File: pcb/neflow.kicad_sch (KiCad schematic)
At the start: 51 parts, among them J1 Temp0, J2 Temp1, J3 SSR0, J4 SSR1, J6 1333870, J7 FAN1, J8 FAN0, Q1 IRLML2502, Q2 IRLML2502, Q3 IRLML2502, Q4 IRLML2502, Q5 IRLML2502, Q6 Q_PMOS_GSD, SW1 SW_Push, SW2 SW_Push, SW3 SW_Push, SW4 SW_Push, U1 MAX31855KASA+T, U2 MAX31855KASA+T, U3 Pico

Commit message: WIP: Switching to workstation
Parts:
- added R1, R11: 10K, Resistor_SMD:R_0603_1608Metric, symbol Device:R_Small
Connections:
- net +3.3V: now also U3.36 (3V3), R1.2, R11.2
- net MAX_SO: now reaches U3.11 (GPIO8)
- net MAX_SO: now also U1.7 (SO), U2.7 (SO)
- net PI_TEMP0_~{CS}: now reaches U3.14 (GPIO10)
- net PI_TEMP0_~{CS}: now also U1.6 (~{CS}), R1.1
- net PI_TEMP1_~{CS}: now reaches U3.15 (GPIO11)
- net PI_TEMP1_~{CS}: now also U2.6 (~{CS}), R11.1
- net SCREEN_SDA: now reaches U3.4 (GPIO2)
- net SCREEN_SDA: now also Brd1.4 (SDA)
- net SCREEN_SCL: now reaches U3.5 (GPIO3)
- net SCREEN_SCL: now also Brd1.3 (SCL)
- net MAX_SCK: now reaches U3.9 (GPIO6)
- net MAX_SCK: now also U1.5 (SCK), U2.5 (SCK)
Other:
- moved on the sheet: C1, C2, C3, C4, C5, C6, FB1, FB2, FB3, FB4, J1, J2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

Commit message: WIP: Working on pcb
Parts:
- J101: renamed from J6; footprint Unsharable:1333870 -> Unshareable:1333870
- JP102: renamed from JP2; value SolderJumper_3_Open -> VSel1
- renumbered Brd1 to Brd101, C7 to C101, C8 to C102, C9 to C103, C10 to C104, C2 to C105, C3 to C106, C5 to C107, C6 to C108, C1 to C109, C4 to C110, D1 to D101, D2 to D102, D3 to D103, FB2 to FB101, FB3 to FB102, FB1 to FB103, FB4 to FB104, J8 to J102, J3 to J103, J7 to J104, J4 to J105, J1 to J106, J2 to J107, JP1 to JP101, LS1 to LS101, PS1 to PS101, Q6 to Q101, Q1 to Q102, Q4 to Q103, Q5 to Q104, Q2 to Q105, Q3 to Q106, R7 to R101, R9 to R102, R2 to R103, R5 to R104, R6 to R105, R8 to R106, R10 to R107, R3 to R108, R4 to R109, R1 to R110, R11 to R111, SW1 to SW101, SW3 to SW102, SW2 to SW103, SW4 to SW104, U3 to U101, U1 to U102, U2 to U103
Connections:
- net BTN0: now also U101.16 (GPIO12)
- net BTN1: now also U101.17 (GPIO13)
- net BTN2: now also U101.19 (GPIO14)
- net BTN3: now also U101.20 (GPIO15)
- net FAN0: now also U101.26 (GPIO20)
- net FAN1: now also U101.27 (GPIO21)
- net SPK: now also U101.21 (GPIO16)
- net SSR0: now also U101.24 (GPIO18)
- net SSR1: now also U101.25 (GPIO19)
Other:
- moved on the sheet: C107, C108, C110, FB102, FB104, J107, R107, R111, SW104, U103

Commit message: WIP: changes to pcb
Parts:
- added H1, H2, H3, H4: MountingHole, MountingHole:MountingHole_3mm, symbol Mechanical:MountingHole
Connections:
- net T0+: now also J106.1 (Pin_1); no longer J106.2 (Pin_2)
- net T0-: now also J106.2 (Pin_2); no longer J106.1 (Pin_1)
- net T1+: now also J107.1 (Pin_1); no longer J107.2 (Pin_2)
- net T1-: now also J107.2 (Pin_2); no longer J107.1 (Pin_1)
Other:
- moved on the sheet: J106, J107, JP102

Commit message: WIP: Finishing the pcb rev0
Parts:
- removed R107: 10K, Resistor_SMD:R_0603_1608Metric, symbol Device:R_Small
- removed SW104: SW_Push, silicone_btn:BUTTON_SILICON, symbol Switch:SW_Push
- added H5, H6, H7, H8: MountingHole, MountingHole:MountingHole_3mm, symbol Mechanical:MountingHole
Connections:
- net BTN3 is gone; now on net SCREEN_SCL: U101.20 (GPIO15)
- net BTN0: now also U101.14 (GPIO10); no longer U101.16 (GPIO12)
- net BTN1: now also U101.15 (GPIO11); no longer U101.17 (GPIO13)
- net BTN2: now also U101.16 (GPIO12); no longer U101.19 (GPIO14)
- net FAN0: now also U101.6 (GPIO4); no longer U101.26 (GPIO20)
- net FAN1: now also U101.7 (GPIO5); no longer U101.27 (GPIO21)
- net GND: now also U101.13 (GND), U101.18 (GND), U101.23 (GND), U101.28 (GND), U101.3 (GND), U101.33 (AGND), U101.38 (GND), U101.42 (GND), U101.8 (GND)
- net PI_TEMP0_~{CS}: now also U101.25 (GPIO19); no longer U101.14 (GPIO10)
- net PI_TEMP1_~{CS}: now also U101.26 (GPIO20); no longer U101.15 (GPIO11)
- net SCREEN_SCL: no longer U101.5 (GPIO3)
- net SCREEN_SDA: now also U101.19 (GPIO14); no longer U101.4 (GPIO2)
- net SPK: now also U101.9 (GPIO6); no longer U101.21 (GPIO16)
- net SSR0: now also U101.4 (GPIO2); no longer U101.24 (GPIO18)
- net SSR1: now also U101.5 (GPIO3); no longer U101.25 (GPIO19)
- net AC/L: now reaches J101.1, J101.3, J101.5, PS101.1 (AC/L)
- net AC/N: now reaches J101.2, J101.4, J101.6, PS101.2 (AC/N)
- net MAX_SCK renamed MAX_SPI_SCK
- net MAX_SPI_SCK: now also U101.24 (GPIO18); no longer U101.9 (GPIO6)
- net MAX_SO renamed MAX_SPI_RX
- net MAX_SPI_RX: now also U101.21 (GPIO16); no longer U101.11 (GPIO8)
- no-connect marks 0 -> 15

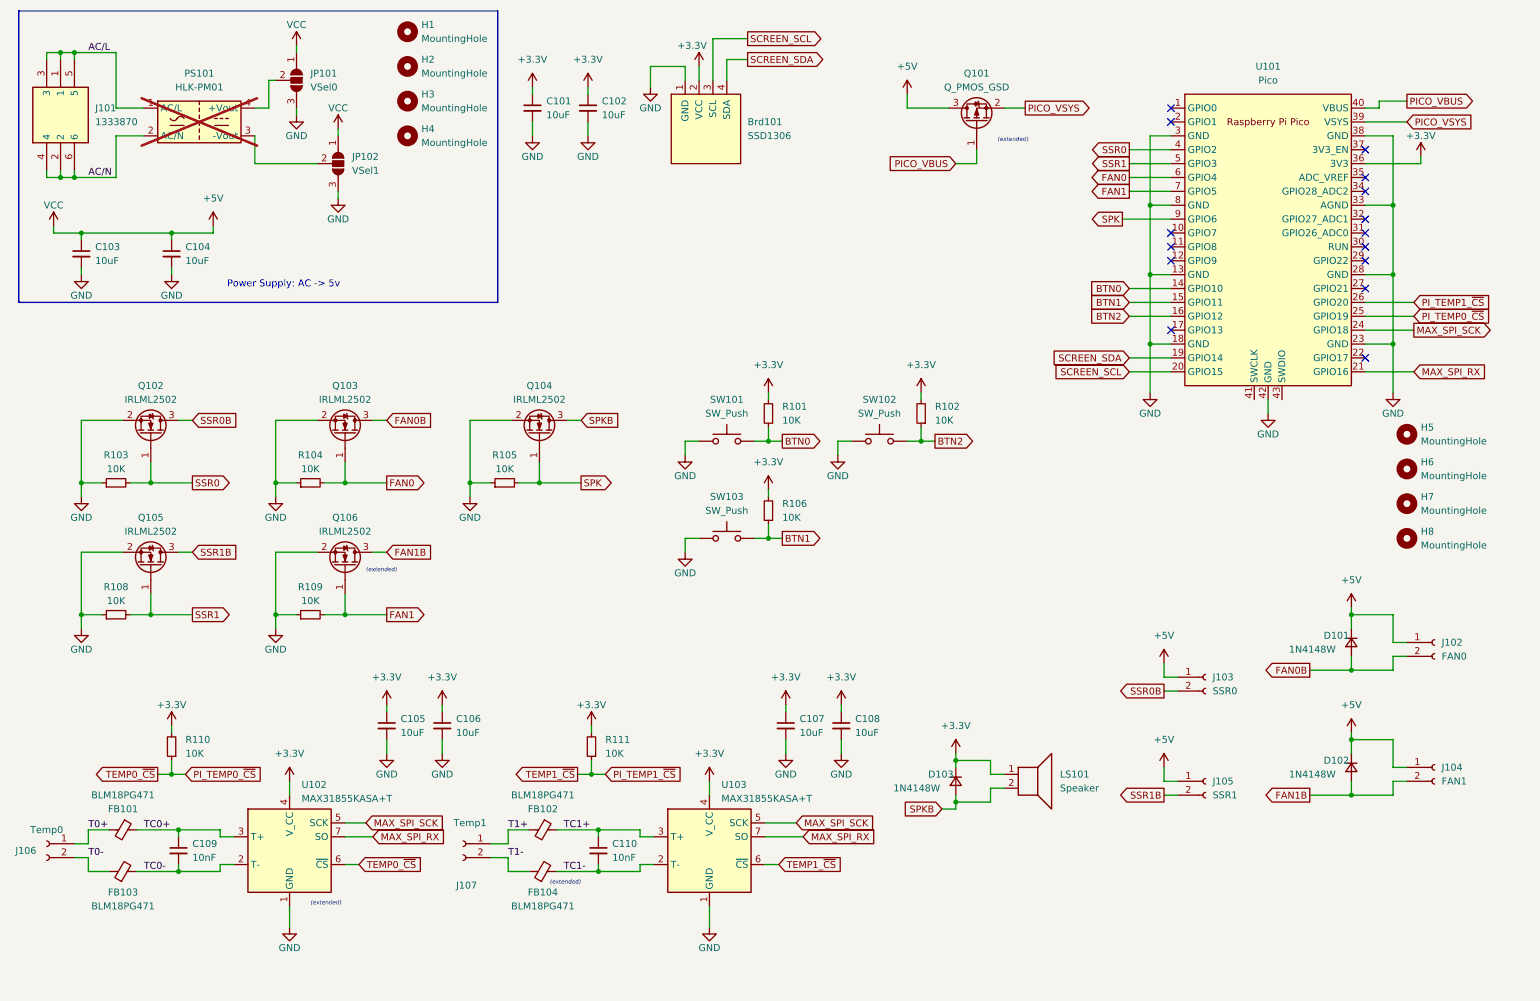
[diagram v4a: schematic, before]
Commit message: Added TLV803E supply voltage supervisor
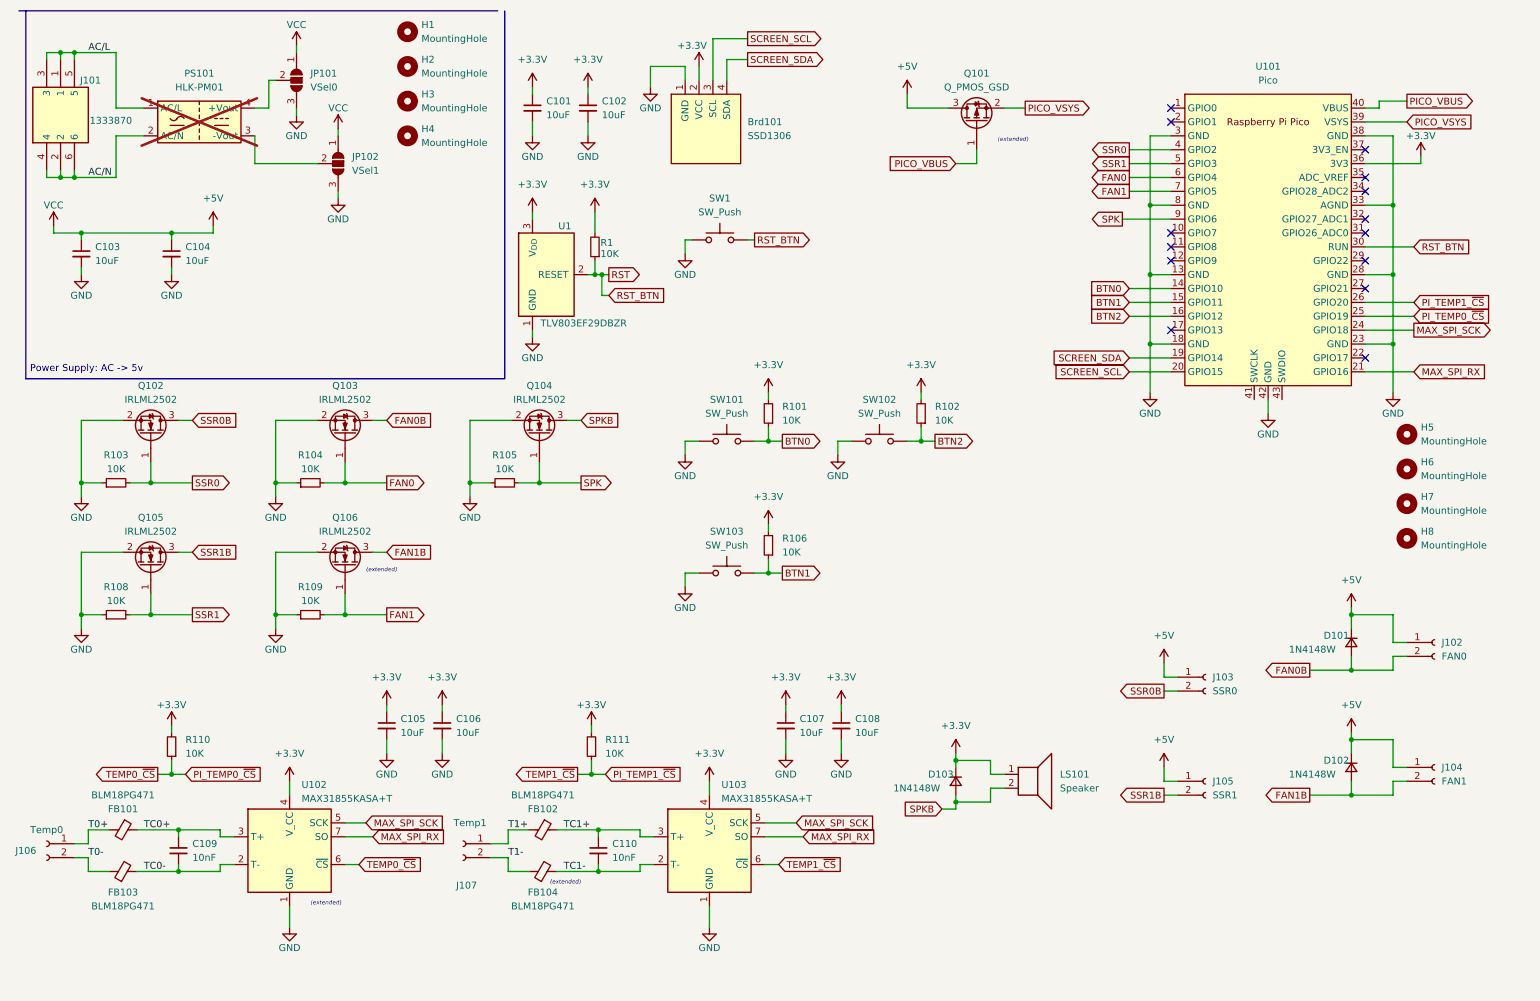
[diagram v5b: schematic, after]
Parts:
- added R1: 10K, Resistor_SMD:R_0603_1608Metric, symbol Device:R_Small
- added SW1: SW_Push, silicone_btn:BUTTON_SILICON, symbol Switch:SW_Push
- added U1: TLV803EF29DBZR, Package_TO_SOT_SMD:SOT-23, symbol Power_Supervisor:TLV810EA29DBZ
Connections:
- net +3.3V: now also R1.2, U1.3 (V_{DD})
- net GND: now also SW1.1, U1.1 (GND)
- net RST: now reaches U101.30 (RUN)
- net RST: now also R1.1, SW1.2, U1.2 (RESET)
- no-connect marks 15 -> 14
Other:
- moved on the sheet: R106, SW103

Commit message: Adding new pcb changes for v2 pcb with reset logic
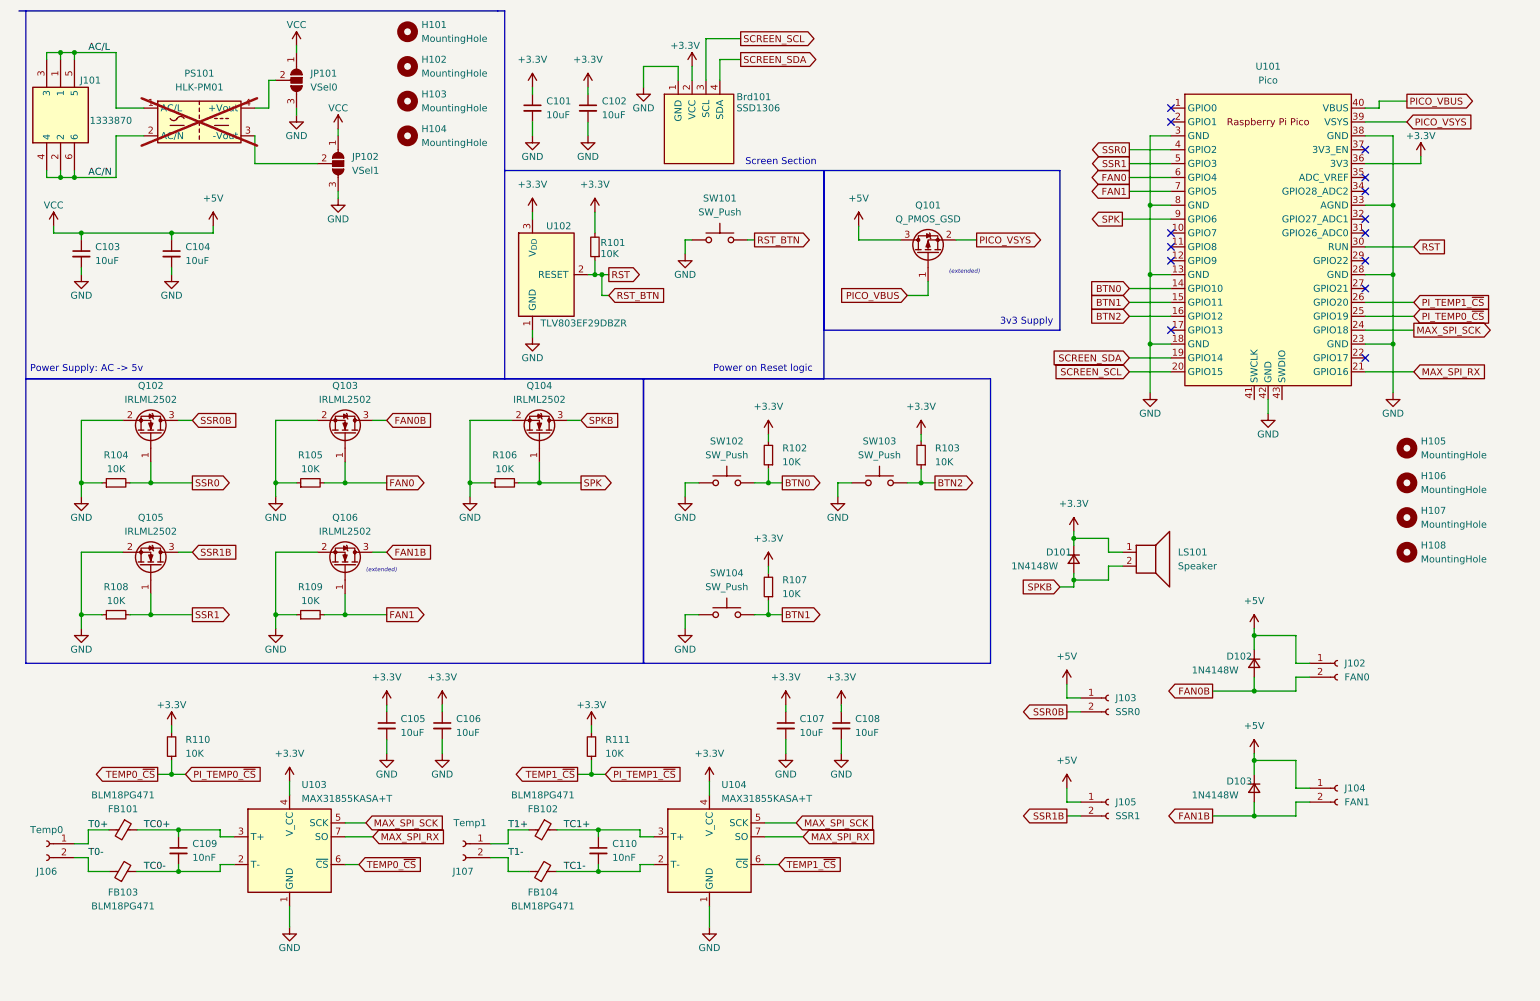
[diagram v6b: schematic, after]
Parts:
- Brd101, LS101, U101: now left out of the parts list
- SW101: renamed from SW1; now left out of the parts list
- SW102: renamed from SW101; now left out of the parts list
- SW103: renamed from SW102; now left out of the parts list
- SW104: renamed from SW103; now left out of the parts list
- renumbered D103 to D101, D101 to D102, D102 to D103, H1 to H101, H2 to H102, H3 to H103, H4 to H104, H5 to H105, H6 to H106, H7 to H107, H8 to H108, R1 to R101, R101 to R102, R102 to R103, R103 to R104, R104 to R105, R105 to R106, R106 to R107, U1 to U102, U102 to U103, U103 to U104
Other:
- note added: "3v3 Supply"
- note added: "Power on Reset logic"
- note added: "Screen Section"
- moved on the sheet: Brd101, D101, D102, D103, H105, H106, H107, H108, J102, J103, J104, J105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
